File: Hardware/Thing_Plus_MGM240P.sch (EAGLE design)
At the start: 97 parts, among them J1 THING_PLUS_LOGICAL, J2 USB Female Type C Connector, J3 QWIIC_RIGHT_ANGLE, J5 MICRO-SDFRICTION, Q1 20V/4.2A/52mΩ/1.4W, U1 MGM240P, U2 XC6222B331MR-G, U3 EFM32GG12B410F1024GL120, U4 MCP73831, U5 MAX17048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

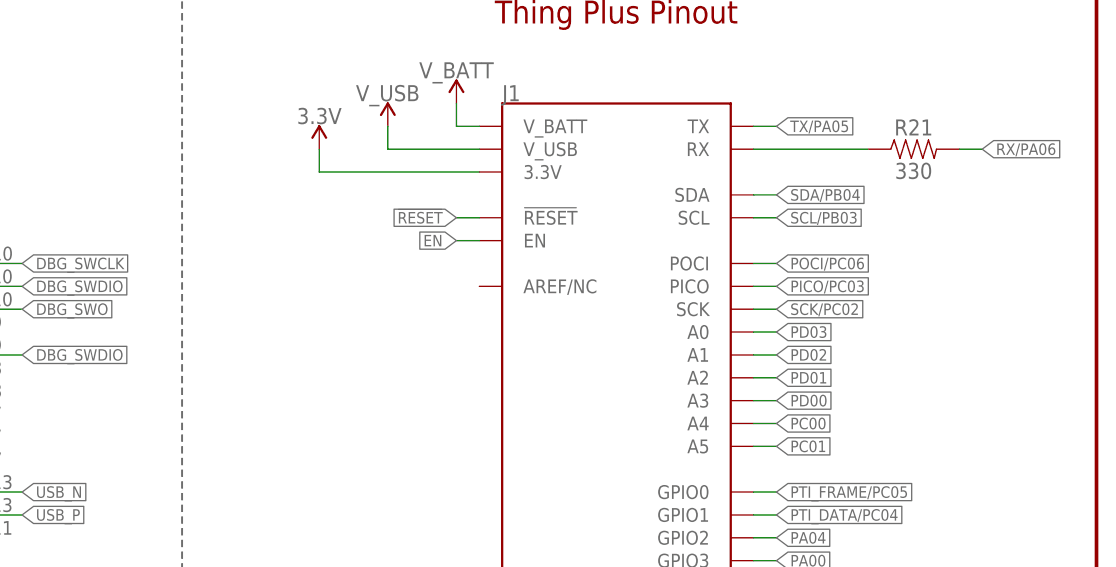
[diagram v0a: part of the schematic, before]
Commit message: Design review updates
Add "ENIG Finish" to ordering instructions
Add jumpers for rerouting reset line to A0 pin
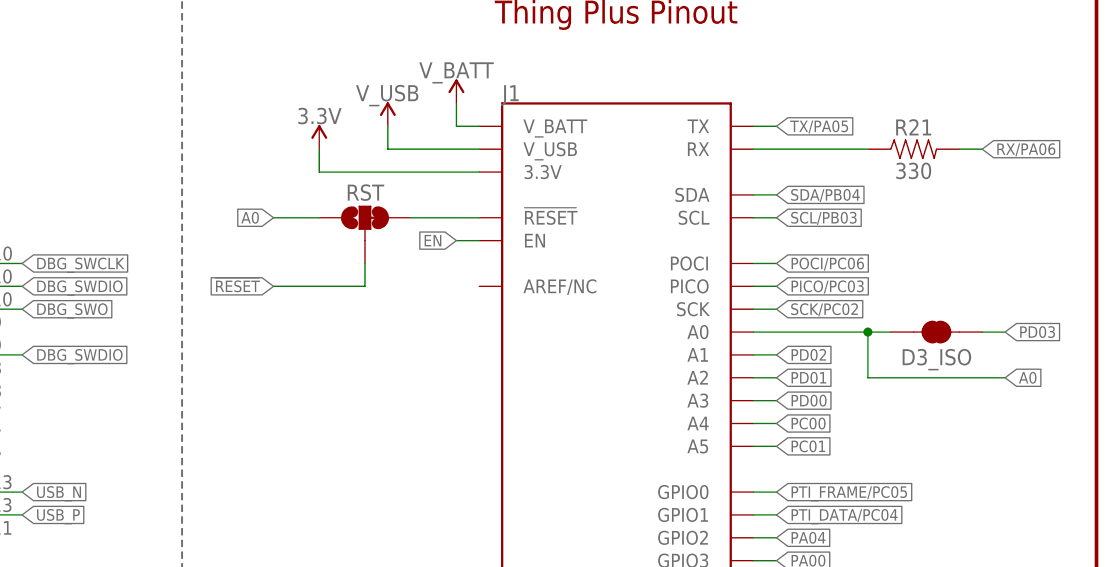
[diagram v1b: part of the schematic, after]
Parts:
- added D3_ISO: JUMPER-SMT_2_NC_TRACE_SILK, SparkFun-Jumpers:JUMPER-SMT_2_NC_TRACE_SILK
- added RST: JUMPER-SMT_3_1-NC_TRACE_SILK, SparkFun-Jumpers:JUMPER-SMT_3_1-NC_TRACE_SILK
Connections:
- new net A0: D3_ISO.2, J1.A0, RST.1
- new net N$28: J1.!RESET, RST.3
- net !RESET!: now also RST.2; no longer J1.!RESET
- net PD03: now also D3_ISO.1; no longer J1.A0
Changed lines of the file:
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@@
 <part name="R20" library="SparkFun-Resistors" deviceset="330OHM" device="-0402T-1/16W-5%" value="330"/>
 <part name="R21" library="SparkFun-Resistors" deviceset="330OHM" device="-0402T-1/16W-5%" value="330"/>
+<part name="RST" library="SparkFun-Jumpers" deviceset="JUMPER-SMT_3_1-NC_TRACE" device="_SILK" package3d_urn="urn:adsk.eagle:package:39288/1"/>
+<part name="D3_ISO" library="SparkFun-Jumpers" deviceset="JUMPER-SMT_2_NC_TRACE" device="_SILK" package3d_urn="urn:adsk.eagle:package:39281/1" value="JUMPER-SMT_2_NC_TRACE_SILK"/>
 </parts>
 <sheets>
@@
 <attribute name="VALUE" x="411.48" y="128.016" size="1.778" layer="96" font="vector" align="top-center"/>
 </instance>
+<instance part="RST" gate="G$1" x="350.52" y="121.92" smashed="yes" rot="R90">
+<attribute name="NAME" x="350.52" y="124.714" size="1.778" layer="95" font="vector" align="center"/>
+</instance>
+<instance part="D3_ISO" gate="G$1" x="414.02" y="109.22" smashed="yes" rot="R180">
+<attribute name="NAME" x="414.02" y="106.426" size="1.778" layer="95" font="vector" rot="R180" align="center"/>
+</instance>
 </instances>
 <busses>
@@
 <net name="PD03" class="0">
 <segment>
-<pinref part="J1" gate="G$1" pin="A0"/>
-<wire x1="393.7" y1="109.22" x2="396.24" y2="109.22" width="0.1524" layer="91"/>
-<label x="396.24" y="109.22" size="1.27" layer="95" font="vector" xref="yes"/>
-</segment>
-<segment>
 <pinref part="U1" gate="G$1" pin="PD03"/>
 <wire x1="27.94" y1="83.82" x2="25.4" y2="83.82" width="0.1524" layer="91"/>
 <label x="25.4" y="83.82" size="1.27" layer="95" font="vector" rot="R180" xref="yes"/>
+</segment>
+<segment>
+<wire x1="419.1" y1="109.22" x2="421.64" y2="109.22" width="0.1524" layer="91"/>
+<label x="421.64" y="109.22" size="1.27" layer="95" font="vector" xref="yes"/>
+<pinref part="D3_ISO" gate="G$1" pin="1"/>
 </segment>
 </net>
@@
 </segment>
 <segment>
-<pinref part="J1" gate="G$1" pin="!RESET"/>
-<wire x1="363.22" y1="121.92" x2="360.68" y2="121.92" width="0.1524" layer="91"/>
-<label x="360.68" y="121.92" size="1.27" layer="95" font="vector" rot="R180" xref="yes"/>
-</segment>
-<segment>
 <pinref part="J7" gate="G$1" pin="3"/>
 <wire x1="180.34" y1="182.88" x2="177.8" y2="182.88" width="0.1524" layer="91"/>
@@
 <wire x1="111.76" y1="109.22" x2="109.22" y2="109.22" width="0.1524" layer="91"/>
 <label x="109.22" y="109.22" size="1.27" layer="95" font="vector" rot="R180" xref="yes"/>
+</segment>
+<segment>
+<label x="340.36" y="114.3" size="1.27" layer="95" font="vector" rot="R180" xref="yes"/>
+<pinref part="RST" gate="G$1" pin="2"/>
+<wire x1="340.36" y1="114.3" x2="350.52" y2="114.3" width="0.1524" layer="91"/>
+<wire x1="350.52" y1="114.3" x2="350.52" y2="116.84" width="0.1524" layer="91"/>
 </segment>
 </net>
@@
 </segment>
 </net>
+<net name="A0" class="0">
+<segment>
+<label x="340.36" y="121.92" size="1.27" layer="95" font="vector" rot="R180" xref="yes"/>
+<pinref part="RST" gate="G$1" pin="1"/>
+<wire x1="345.44" y1="121.92" x2="340.36" y2="121.92" width="0.1524" layer="91"/>
+</segment>
+<segment>
+<pinref part="D3_ISO" gate="G$1" pin="2"/>
+<pinref part="J1" gate="G$1" pin="A0"/>
+<wire x1="393.7" y1="109.22" x2="406.4" y2="109.22" width="0.1524" layer="91"/>
+<wire x1="406.4" y1="109.22" x2="408.94" y2="109.22" width="0.1524" layer="91"/>
+<wire x1="406.4" y1="109.22" x2="406.4" y2="104.14" width="0.1524" layer="91"/>
+<junction x="406.4" y="109.22"/>
+<wire x1="406.4" y1="104.14" x2="421.64" y2="104.14" width="0.1524" layer="91"/>
+<label x="421.64" y="104.14" size="1.27" layer="95" font="vector" xref="yes"/>
+</segment>
+</net>
+<net name="N$28" class="0">
+<segment>
+<pinref part="RST" gate="G$1" pin="3"/>
+<pinref part="J1" gate="G$1" pin="!RESET"/>
+<wire x1="355.6" y1="121.92" x2="363.22" y2="121.92" width="0.1524" layer="91"/>
+</segment>
+</net>

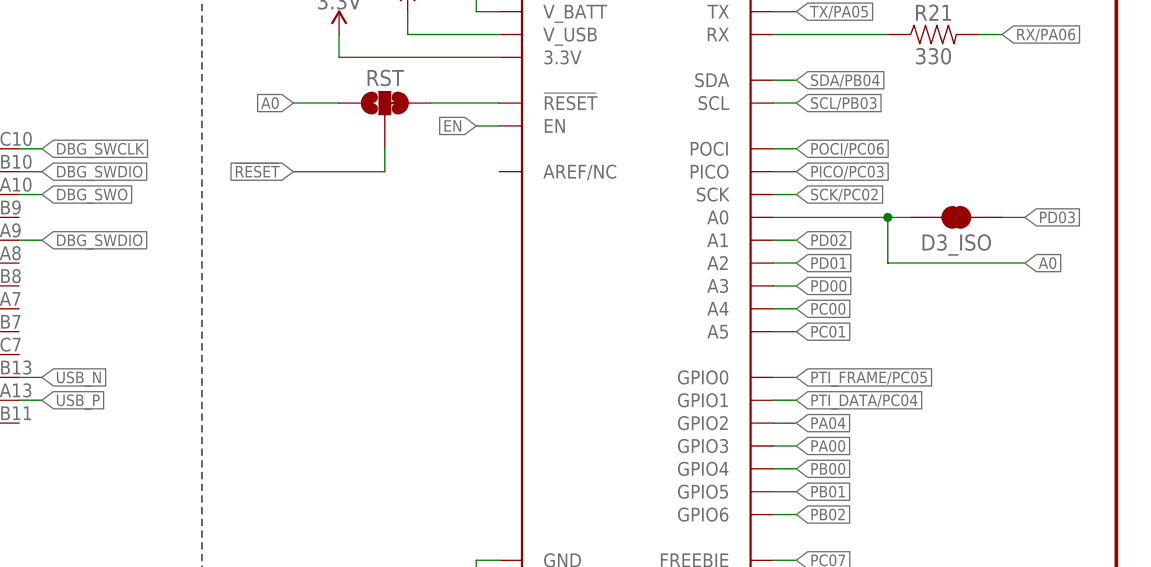
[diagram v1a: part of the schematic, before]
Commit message: Add text to RST and D3_ISO jumpers
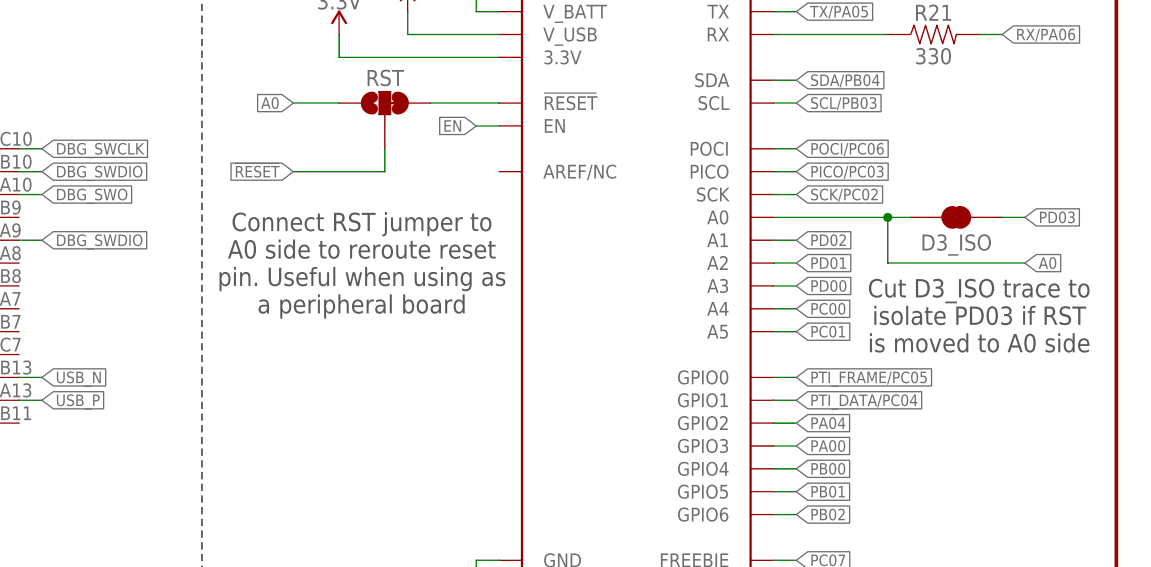
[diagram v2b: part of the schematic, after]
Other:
- note added: "Connect RST jumper to A0 side to reroute reset pin. Useful when using as a peripheral board"
- note added: "Cut D3_ISO trace to isolate PD03 if RST is moved to A0 side"
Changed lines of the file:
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@@
 debugger into low
 power mode</text>
+<text x="347.98" y="104.14" size="2.032" layer="97" font="vector" rot="R180" align="center">Connect RST jumper to
+A0 side to reroute reset
+pin. Useful when using as
+a peripheral board</text>
+<text x="416.56" y="98.298" size="2.032" layer="97" font="vector" rot="R180" align="center">Cut D3_ISO trace to
+isolate PD03 if RST
+is moved to A0 side</text>
 </plain>
 <instances>

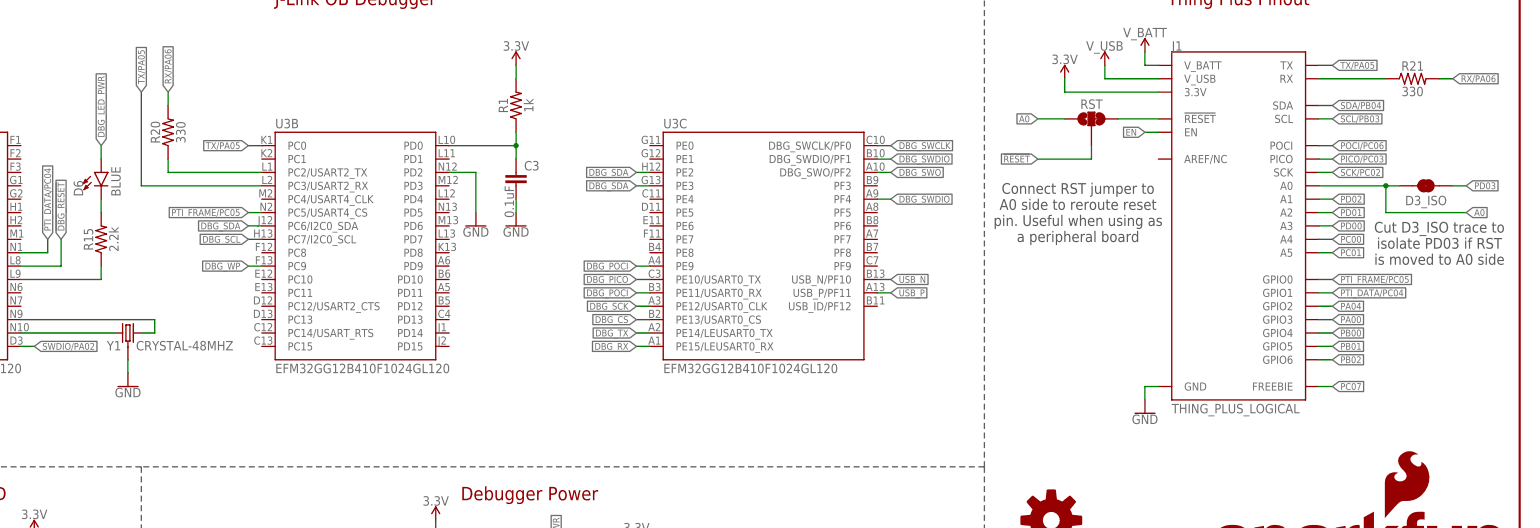
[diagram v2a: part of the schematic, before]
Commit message: Design review updates
Nudge RX/PA06 away from N$25
Add text to schematic explaining escape routing connections
Change RST jumper to "JP1" to make people read the docs
Remove "Thing Plus" from bottom silkscreen
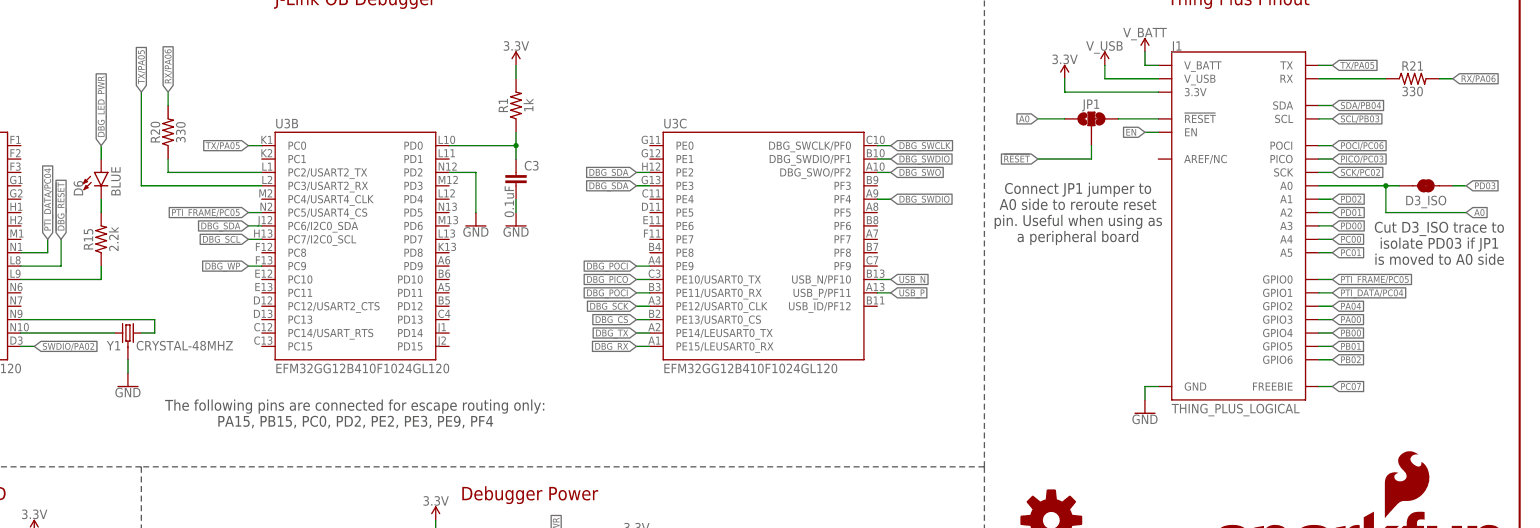
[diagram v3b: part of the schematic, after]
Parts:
- renumbered RST to JP1
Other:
- note added: "Connect JP1 jumper to A0 side to reroute reset pin. Useful when using as a peripheral board"
- note added: "Cut D3_ISO trace to isolate PD03 if JP1 is moved to A0 side"
- note added: "The following pins are connected for escape routing only: PA15, PB15, PC0, PD2, PE2, PE3, PE9, PF4"
- note removed: "Connect RST jumper to A0 side to reroute reset pin. Useful when using as a peripheral board"
- note removed: "Cut D3_ISO trace to isolate PD03 if RST is moved to A0 side"
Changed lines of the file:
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@@
 <part name="R20" library="SparkFun-Resistors" deviceset="330OHM" device="-0402T-1/16W-5%" value="330"/>
 <part name="R21" library="SparkFun-Resistors" deviceset="330OHM" device="-0402T-1/16W-5%" value="330"/>
-<part name="RST" library="SparkFun-Jumpers" deviceset="JUMPER-SMT_3_1-NC_TRACE" device="_SILK" package3d_urn="urn:adsk.eagle:package:39288/1"/>
+<part name="JP1" library="SparkFun-Jumpers" deviceset="JUMPER-SMT_3_1-NC_TRACE" device="_SILK" package3d_urn="urn:adsk.eagle:package:39288/1"/>
 <part name="D3_ISO" library="SparkFun-Jumpers" deviceset="JUMPER-SMT_2_NC_TRACE" device="_SILK" package3d_urn="urn:adsk.eagle:package:39281/1" value="JUMPER-SMT_2_NC_TRACE_SILK"/>
 </parts>
@@
 debugger into low
 power mode</text>
-<text x="347.98" y="104.14" size="2.032" layer="97" font="vector" rot="R180" align="center">Connect RST jumper to
+<text x="347.98" y="104.14" size="2.032" layer="97" font="vector" rot="R180" align="center">Connect JP1 jumper to
 A0 side to reroute reset
 pin. Useful when using as
 a peripheral board</text>
 <text x="416.56" y="98.298" size="2.032" layer="97" font="vector" rot="R180" align="center">Cut D3_ISO trace to
-isolate PD03 if RST
+isolate PD03 if JP1
 is moved to A0 side</text>
+<text x="210.82" y="66.04" size="2.032" layer="97" font="vector" rot="R180" align="center">The following pins are connected for escape routing only:
+PA15, PB15, PC0, PD2, PE2, PE3, PE9, PF4</text>
 </plain>
 <instances>
@@
 <attribute name="VALUE" x="411.48" y="128.016" size="1.778" layer="96" font="vector" align="top-center"/>
 </instance>
-<instance part="RST" gate="G$1" x="350.52" y="121.92" smashed="yes" rot="R90">
+<instance part="JP1" gate="G$1" x="350.52" y="121.92" smashed="yes" rot="R90">
 <attribute name="NAME" x="350.52" y="124.714" size="1.778" layer="95" font="vector" align="center"/>
 </instance>
@@
 <segment>
 <label x="340.36" y="114.3" size="1.27" layer="95" font="vector" rot="R180" xref="yes"/>
-<pinref part="RST" gate="G$1" pin="2"/>
+<pinref part="JP1" gate="G$1" pin="2"/>
 <wire x1="340.36" y1="114.3" x2="350.52" y2="114.3" width="0.1524" layer="91"/>
 <wire x1="350.52" y1="114.3" x2="350.52" y2="116.84" width="0.1524" layer="91"/>
@@
 <segment>
 <label x="340.36" y="121.92" size="1.27" layer="95" font="vector" rot="R180" xref="yes"/>
-<pinref part="RST" gate="G$1" pin="1"/>
+<pinref part="JP1" gate="G$1" pin="1"/>
 <wire x1="345.44" y1="121.92" x2="340.36" y2="121.92" width="0.1524" layer="91"/>
 </segment>
@@
 <net name="N$28" class="0">
 <segment>
-<pinref part="RST" gate="G$1" pin="3"/>
+<pinref part="JP1" gate="G$1" pin="3"/>
 <pinref part="J1" gate="G$1" pin="!RESET"/>
 <wire x1="355.6" y1="121.92" x2="363.22" y2="121.92" width="0.1524" layer="91"/>

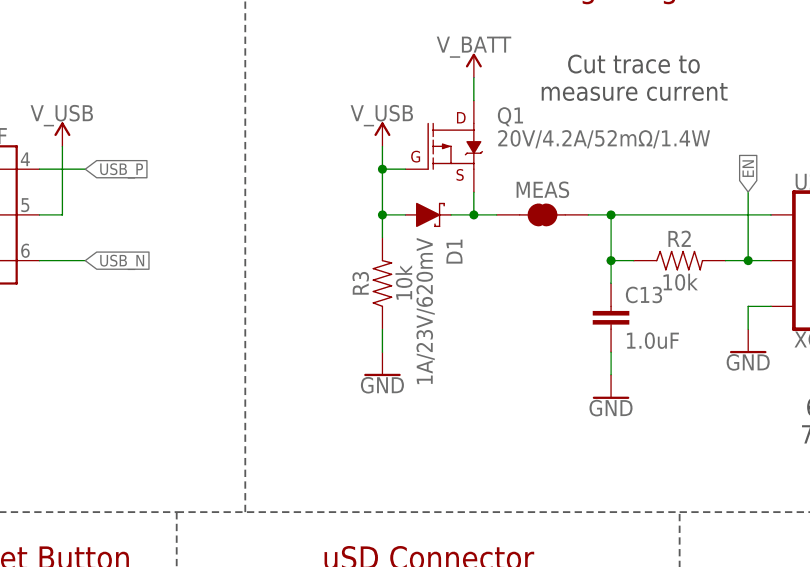
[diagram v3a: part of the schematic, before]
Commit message: Change R3 from 10k to 100k
Improves low power consumption
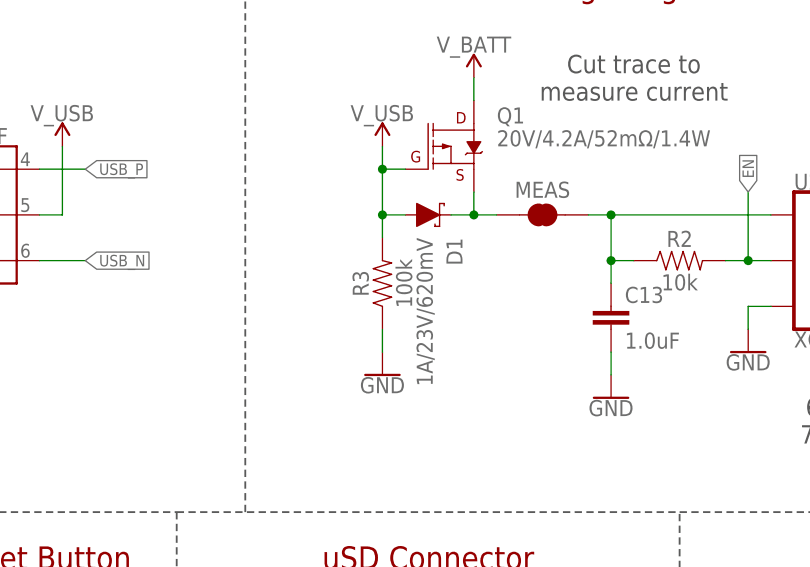
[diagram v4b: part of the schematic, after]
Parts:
- R3: value 10k -> 100k; device SparkFun-Resistors:10KOHM-0402T-1/16W-1% -> SparkFun-Resistors:100KOHM-0402T-1/16W-1%
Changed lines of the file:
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@@
 <part name="D1" library="SparkFun-DiscreteSemi" deviceset="DIODE-SCHOTTKY" device="-BAT20J" value="1A/23V/620mV"/>
 <part name="SUPPLY15" library="SparkFun-PowerSymbols" deviceset="V_USB" device=""/>
-<part name="R3" library="SparkFun-Resistors" deviceset="10KOHM" device="-0402T-1/16W-1%" value="10k"/>
+<part name="R3" library="SparkFun-Resistors" deviceset="100KOHM" device="-0402T-1/16W-1%" value="100k"/>
 <part name="GND26" library="SparkFun-PowerSymbols" deviceset="GND" device=""/>
 <part name="C14" library="SparkFun-Capacitors" deviceset="2.2UF" device="-0402_TIGHT-10V-10%-X5R" value="2.2uF"/>
